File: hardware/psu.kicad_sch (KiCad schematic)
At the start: 59 parts, among them IC301 TLV61220DBVT, J301 54-00125, J302 Conn_01x03, Q301 CSD87503Q3E, Q302 CSD87503Q3E, Q303 Q_NMOS, U301 TPS63020DSJR, U302 BQ25798RQMR

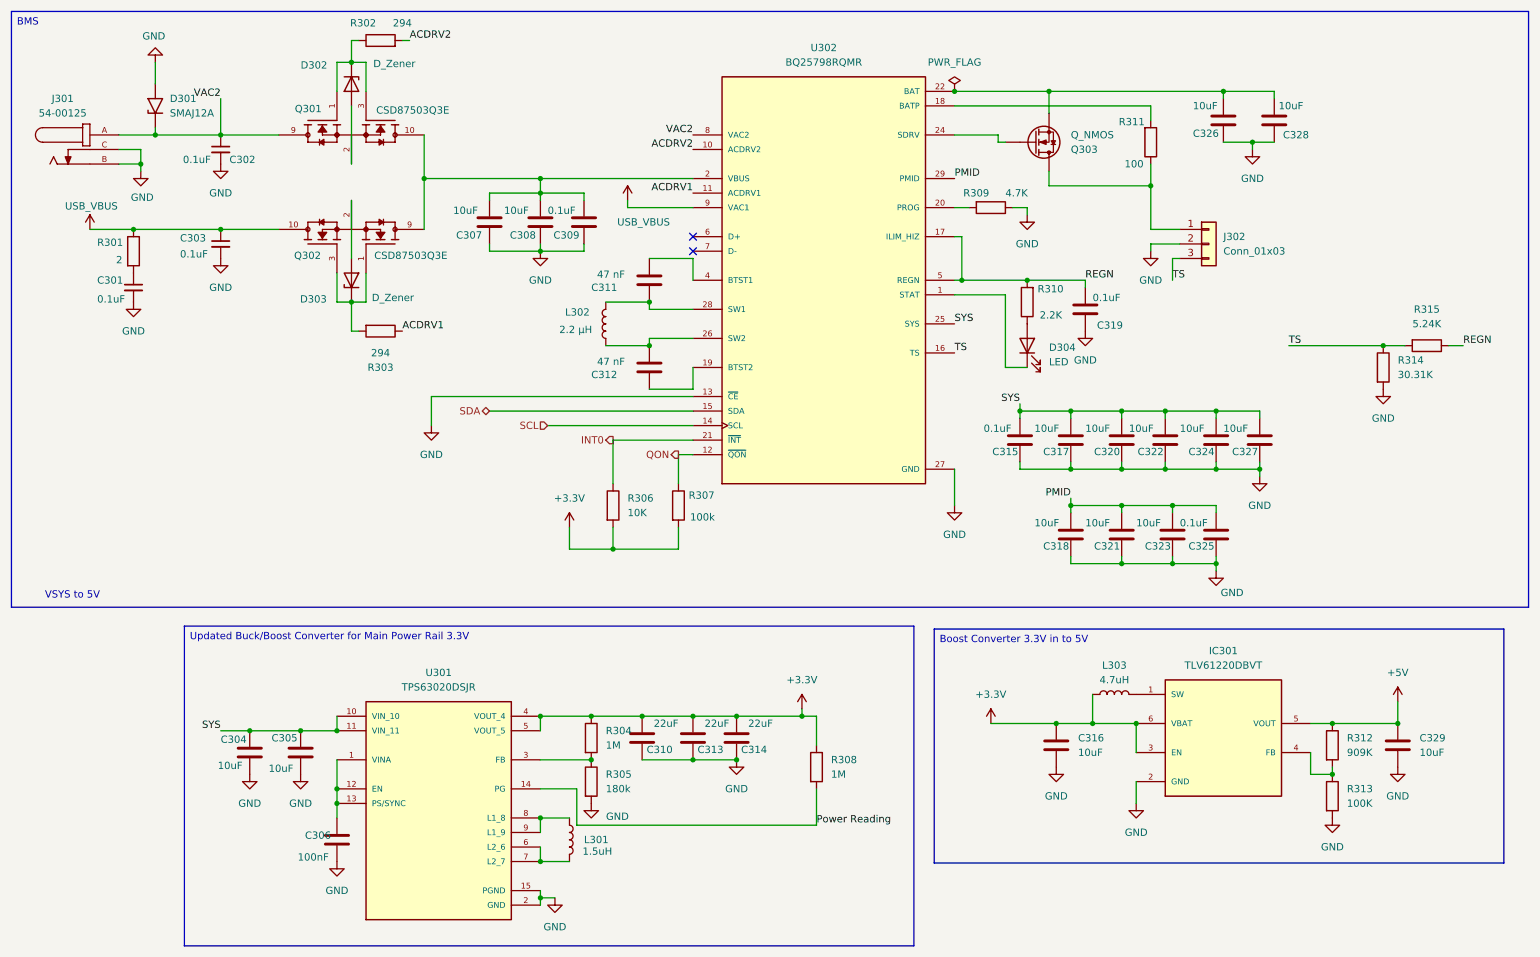
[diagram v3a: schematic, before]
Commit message: updated labels
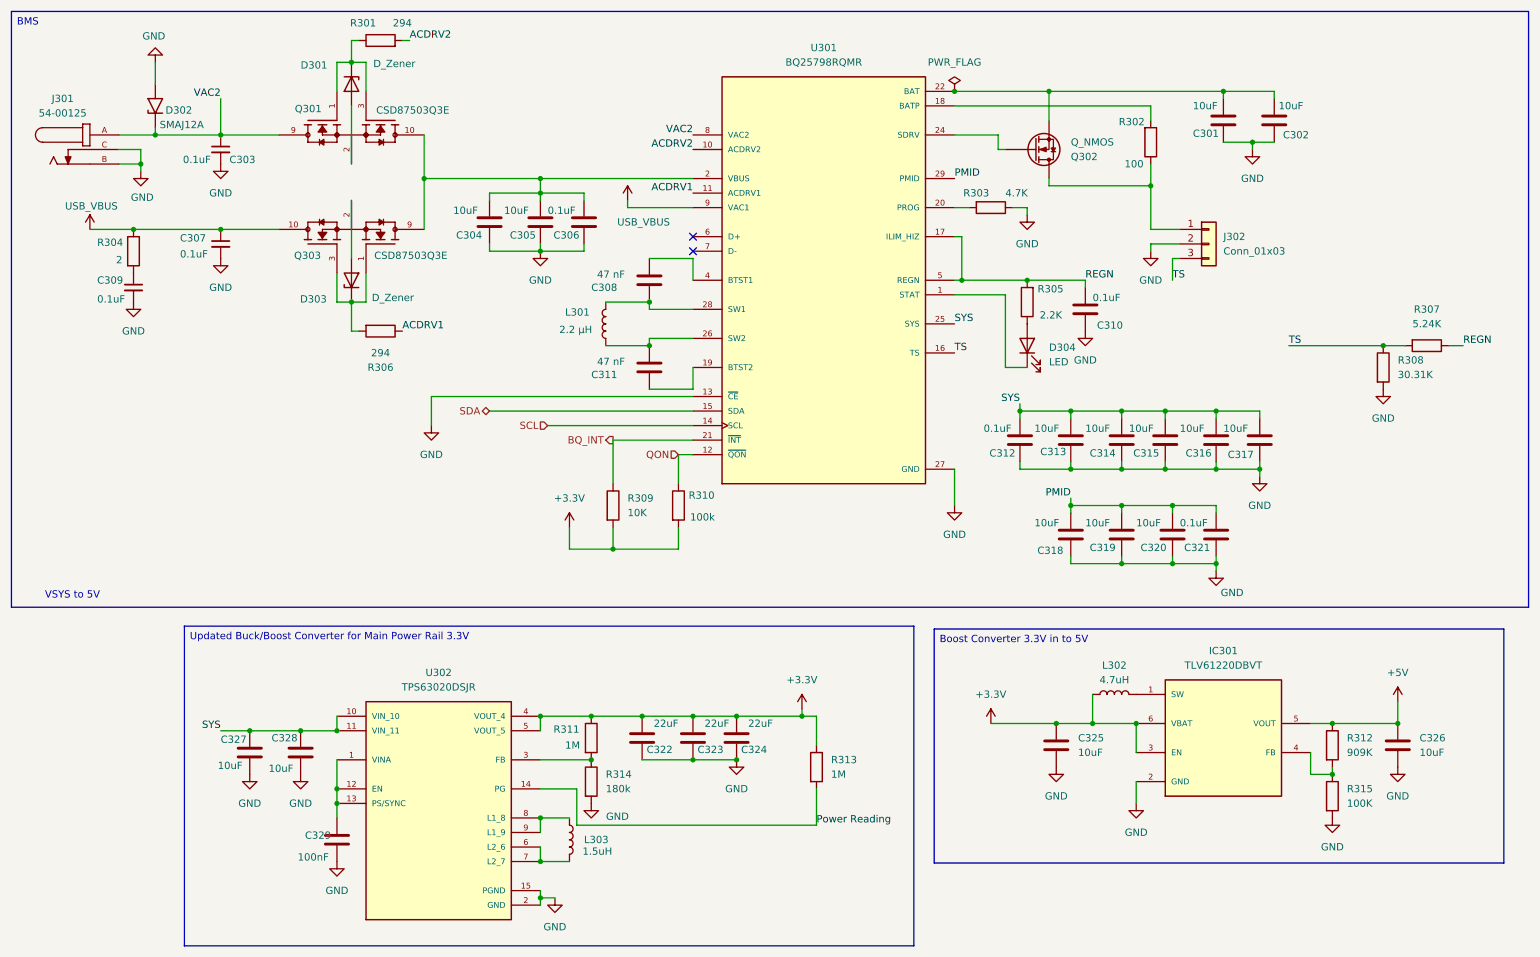
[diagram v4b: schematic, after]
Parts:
- renumbered C326 to C301, C328 to C302, C302 to C303, C307 to C304, C308 to C305, C309 to C306, C303 to C307, C311 to C308, C301 to C309, C319 to C310, C312 to C311, C315 to C312, C317 to C313, C320 to C314, C322 to C315, C324 to C316, C327 to C317, C321 to C319, C323 to C320, C325 to C321, C310 to C322, C313 to C323, C314 to C324, C316 to C325, C329 to C326, C304 to C327, C305 to C328, C306 to C329, D302 to D301, D301 to D302, L302 to L301, L303 to L302, L301 to L303, Q303 to Q302, Q302 to Q303, R302 to R301, R311 to R302, R309 to R303, R301 to R304, R310 to R305, R303 to R306, R315 to R307, R314 to R308, R306 to R309, R307 to R310, R304 to R311, R308 to R313, R305 to R314, R313 to R315, U302 to U301, U301 to U302
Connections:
- net INT0 renamed BQ_INT
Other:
- moved on the sheet: Q302

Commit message: reannotate
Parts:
- renumbered C301 to C201, C302 to C202, C303 to C203, C304 to C204, C305 to C205, C306 to C206, C307 to C207, C308 to C208, C309 to C209, C310 to C210, C311 to C211, C312 to C212, C313 to C213, C314 to C214, C315 to C215, C316 to C216, C317 to C217, C318 to C218, C319 to C219, C320 to C220, C321 to C221, C322 to C222, C323 to C223, C324 to C224, C325 to C225, C326 to C226, C327 to C227, C328 to C228, C329 to C229, D301 to D201, D302 to D202, D303 to D203, D304 to D204, IC301 to IC201, J301 to J201, J302 to J202, L301 to L201, L302 to L202, L303 to L203, Q301 to Q201, Q302 to Q202, Q303 to Q203, R301 to R201, R302 to R202, R303 to R203, R304 to R204, R305 to R205, R306 to R206, R307 to R207, R308 to R208, R309 to R209, R310 to R210, R311 to R211, R312 to R212, R313 to R213, R314 to R214, R315 to R215, U301 to U201, U302 to U202

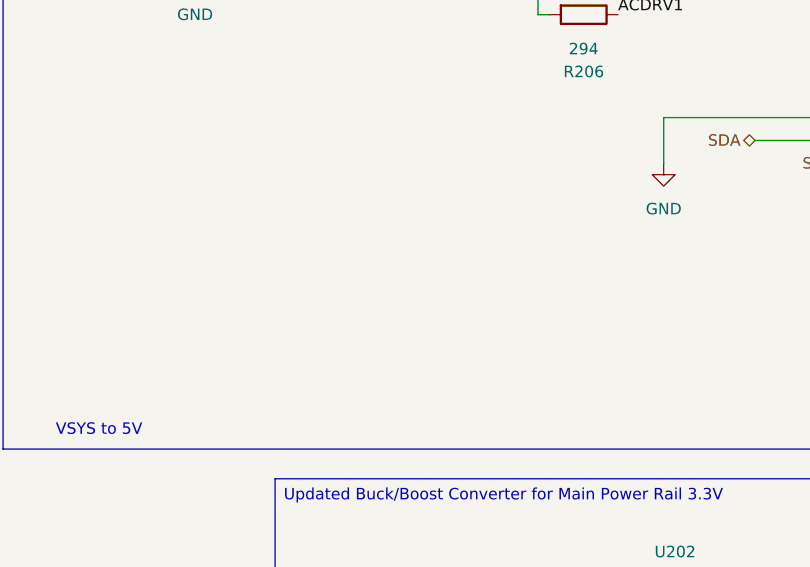
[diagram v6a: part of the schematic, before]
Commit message: added QON pushbutton
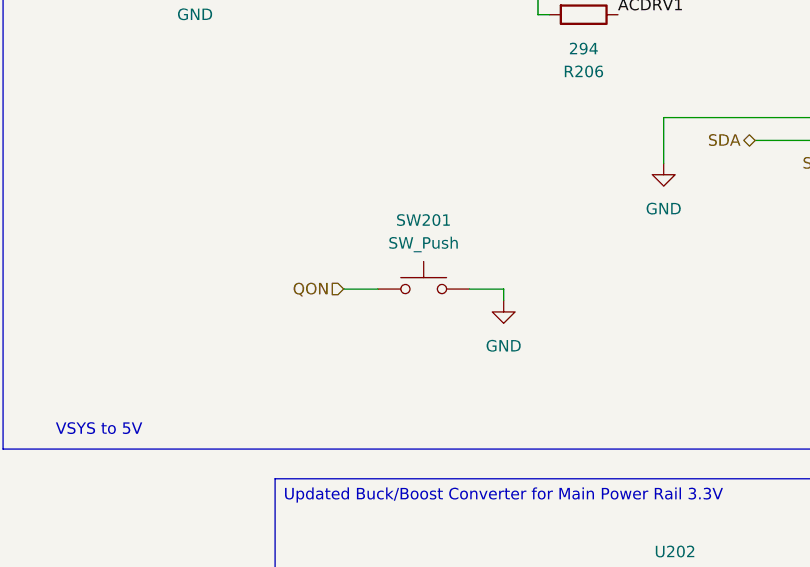
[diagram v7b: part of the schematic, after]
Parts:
- added SW201: SW_Push, symbol Switch:SW_Push
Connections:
- net GND: now also SW201.2
- net QON: now also SW201.1
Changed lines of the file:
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@@
 	(wire
 		(pts
+			(xy 67.31 100.33) (xy 71.12 100.33)
+		)
+		(stroke
+			(width 0)
+			(type default)
+		)
+	)
+	(wire
+		(pts
 			(xy 226.06 110.49) (xy 226.06 111.76)
 		)
@@
 	(wire
 		(pts
+			(xy 53.34 100.33) (xy 57.15 100.33)
+		)
+		(stroke
+			(width 0)
+			(type default)
+		)
+	)
+	(wire
+		(pts
 			(xy 217.17 93.98) (xy 226.06 93.98)
 		)
@@
 	(wire
 		(pts
+			(xy 71.12 100.33) (xy 71.12 101.6)
+		)
+		(stroke
+			(width 0)
+			(type default)
+		)
+	)
+	(wire
+		(pts
 			(xy 218.44 57.15) (xy 219.71 57.15)
 		)
@@
 		)
 	)
+	(hierarchical_label "QON"
+		(shape input)
+		(at 53.34 100.33 180)
+		(effects
+			(font
+				(size 1.27 1.27)
+			)
+			(justify right)
+		)
+	)
 	(symbol
 		(lib_id "Device:C")
@@
 	)
 	(symbol
+		(lib_id "power:GND")
+		(at 71.12 101.6 0)
+		(unit 1)
+		(exclude_from_sim no)
+		(in_bom yes)
+		(on_board yes)
+		(dnp no)
+		(fields_autoplaced yes)
+		(property "Reference" "#PWR0217"
+			(at 71.12 107.95 0)
+			(effects
+				(font
+					(size 1.27 1.27)
+				)
+				(hide yes)
+			)
+		)
+		(property "Value" "GND"
+			(at 71.12 106.68 0)
+			(effects
+				(font
+					(size 1.27 1.27)
+				)
+			)
+		)
+		(property "Footprint" ""
+			(at 71.12 101.6 0)
+			(effects
+				(font
+					(size 1.27 1.27)
+				)
+				(hide yes)
+			)
+		)
+		(property "Datasheet" ""
+			(at 71.12 101.6 0)
+			(effects
+				(font
+					(size 1.27 1.27)
+				)
+				(hide yes)
+			)
+		)
+		(property "Description" "Power symbol creates a global label with name \"GND\" , ground"
+			(at 71.12 101.6 0)
+			(effects
+				(font
+					(size 1.27 1.27)
+				)
+				(hide yes)
+			)
+		)
+		(pin "1"
+		)
+		(instances
+			(project "Senior_Design"
+				(path "/8f5928e8-0fc1-4443-a20f-3bfeb956761e/09dae378-4d12-4dca-bc21-c216f94ec21f"
+					(reference "#PWR0217")
+					(unit 1)
+				)
+			)
+		)
+	)
+	(symbol
 		(lib_id "Device:C_Small")
 		(at 52.07 38.1 0)
@@
 		(dnp no)
 		(fields_autoplaced yes)
-		(property "Reference" "#PWR0230"
+		(property "Reference" "#PWR0231"
 			(at 72.39 168.91 0)
 			(effects
@@
 			(project "Senior_Design"
 				(path "/8f5928e8-0fc1-4443-a20f-3bfeb956761e/09dae378-4d12-4dca-bc21-c216f94ec21f"
-					(reference "#PWR0230")
+					(reference "#PWR0231")
 					(unit 1)
 				)
@@
 		(dnp no)
 		(fields_autoplaced yes)
-		(property "Reference" "#PWR0228"
+		(property "Reference" "#PWR0229"
 			(at 212.09 158.75 0)
 			(effects
@@
 			(project "Senior_Design"
 				(path "/8f5928e8-0fc1-4443-a20f-3bfeb956761e/09dae378-4d12-4dca-bc21-c216f94ec21f"
-					(reference "#PWR0228")
+					(reference "#PWR0229")
 					(unit 1)
 				)
@@
 		(on_board yes)
 		(dnp no)
-		(property "Reference" "#PWR0218"
+		(property "Reference" "#PWR0219"
 			(at 226.06 118.11 0)
 			(effects
@@
 			(project "Senior_Design"
 				(path "/8f5928e8-0fc1-4443-a20f-3bfeb956761e/09dae378-4d12-4dca-bc21-c216f94ec21f"
-					(reference "#PWR0218")
+					(reference "#PWR0219")
 					(unit 1)
 				)
@@
 		(dnp no)
 		(fields_autoplaced yes)
-		(property "Reference" "#PWR0222"
+		(property "Reference" "#PWR0223"
 			(at 142.24 151.13 0)
 			(effects
@@
 			(project "Senior_Design"
 				(path "/8f5928e8-0fc1-4443-a20f-3bfeb956761e/09dae378-4d12-4dca-bc21-c216f94ec21f"
-					(reference "#PWR0222")
+					(reference "#PWR0223")
 					(unit 1)
 				)
@@
 		(dnp no)
 		(fields_autoplaced yes)
-		(property "Reference" "#PWR0221"
+		(property "Reference" "#PWR0222"
 			(at 186.69 142.24 0)
 			(effects
@@
 			(project "Senior_Design"
 				(path "/8f5928e8-0fc1-4443-a20f-3bfeb956761e/09dae378-4d12-4dca-bc21-c216f94ec21f"
-					(reference "#PWR0221")
+					(reference "#PWR0222")
 					(unit 1)
 				)
@@
 		(dnp no)
 		(fields_autoplaced yes)
-		(property "Reference" "#PWR0226"
+		(property "Reference" "#PWR0227"
 			(at 66.04 153.67 0)
 			(effects
@@
 			(project "Senior_Design"
 				(path "/8f5928e8-0fc1-4443-a20f-3bfeb956761e/09dae378-4d12-4dca-bc21-c216f94ec21f"
-					(reference "#PWR0226")
+					(reference "#PWR0227")
 					(unit 1)
 				)
@@
 		(dnp no)
 		(fields_autoplaced yes)
-		(property "Reference" "#PWR0219"
+		(property "Reference" "#PWR0220"
 			(at 257.81 138.43 0)
 			(effects
@@
 			(project ""
 				(path "/8f5928e8-0fc1-4443-a20f-3bfeb956761e/09dae378-4d12-4dca-bc21-c216f94ec21f"
-					(reference "#PWR0219")
+					(reference "#PWR0220")
 					(unit 1)
 				)
@@
 		(dnp no)
 		(fields_autoplaced yes)
-		(property "Reference" "#PWR0229"
+		(property "Reference" "#PWR0230"
 			(at 246.38 161.29 0)
 			(effects
@@
 			(project "Senior_Design"
 				(path "/8f5928e8-0fc1-4443-a20f-3bfeb956761e/09dae378-4d12-4dca-bc21-c216f94ec21f"
-					(reference "#PWR0229")
+					(reference "#PWR0230")
 					(unit 1)
 				)
@@
 		(dnp no)
 		(fields_autoplaced yes)
-		(property "Reference" "#PWR0231"
+		(property "Reference" "#PWR0232"
 			(at 110.49 175.26 0)
 			(effects
@@
 			(project "Senior_Design"
 				(path "/8f5928e8-0fc1-4443-a20f-3bfeb956761e/09dae378-4d12-4dca-bc21-c216f94ec21f"
-					(reference "#PWR0231")
+					(reference "#PWR0232")
 					(unit 1)
 				)
@@
 	)
 	(symbol
+		(lib_id "Switch:SW_Push")
+		(at 62.23 100.33 0)
+		(unit 1)
+		(exclude_from_sim no)
+		(in_bom yes)
+		(on_board yes)
+		(dnp no)
+		(fields_autoplaced yes)
+		(property "Reference" "SW201"
+			(at 62.23 92.71 0)
+			(effects
+				(font
+					(size 1.27 1.27)
+				)
+			)
+		)
+		(property "Value" "SW_Push"
+			(at 62.23 95.25 0)
+			(effects
+				(font
+					(size 1.27 1.27)
+				)
+			)
+		)
+		(property "Footprint" ""
+			(at 62.23 95.25 0)
+			(effects
+				(font
+					(size 1.27 1.27)
+				)
+				(hide yes)
+			)
+		)
+		(property "Datasheet" "~"
+			(at 62.23 95.25 0)
+			(effects
+				(font
+					(size 1.27 1.27)
+				)
+				(hide yes)
+			)
+		)
+		(property "Description" "Push button switch, generic, two pins"
+			(at 62.23 100.33 0)
+			(effects
+				(font
+					(size 1.27 1.27)
+				)
+				(hide yes)
+			)
+		)
+		(pin "2"
+		)
+		(pin "1"
+		)
+		(instances
+			(project ""
+				(path "/8f5928e8-0fc1-4443-a20f-3bfeb956761e/09dae378-4d12-4dca-bc21-c216f94ec21f"
+					(reference "SW201")
+					(unit 1)
+				)
+			)
+		)
+	)
+	(symbol
 		(lib_id "power:+3.3V")
 		(at 153.67 135.89 0)
@@
 		(dnp no)
 		(fields_autoplaced yes)
-		(property "Reference" "#PWR0220"
+		(property "Reference" "#PWR0221"
 			(at 153.67 139.7 0)
 			(effects
@@
 			(project "Senior_Design"
 				(path "/8f5928e8-0fc1-4443-a20f-3bfeb956761e/09dae378-4d12-4dca-bc21-c216f94ec21f"
-					(reference "#PWR0220")
+					(reference "#PWR0221")
 					(unit 1)
 				)
@@
 		(dnp no)
 		(fields_autoplaced yes)
-		(property "Reference" "#PWR0224"
+		(property "Reference" "#PWR0225"
 			(at 257.81 152.4 0)
 			(effects
@@
 			(project "Senior_Design"
 				(path "/8f5928e8-0fc1-4443-a20f-3bfeb956761e/09dae378-4d12-4dca-bc21-c216f94ec21f"
-					(reference "#PWR0224")
+					(reference "#PWR0225")
 					(unit 1)
 				)
@@
 		(dnp no)
 		(fields_autoplaced yes)
-		(property "Reference" "#PWR0225"
+		(property "Reference" "#PWR0226"
 			(at 57.15 153.67 0)
 			(effects
@@
 			(project "Senior_Design"
 				(path "/8f5928e8-0fc1-4443-a20f-3bfeb956761e/09dae378-4d12-4dca-bc21-c216f94ec21f"
-					(reference "#PWR0225")
+					(reference "#PWR0226")
 					(unit 1)
 				)
@@
 		(dnp no)
 		(fields_autoplaced yes)
-		(property "Reference" "#PWR0223"
+		(property "Reference" "#PWR0224"
 			(at 198.12 152.4 0)
 			(effects
@@
 			(project "Senior_Design"
 				(path "/8f5928e8-0fc1-4443-a20f-3bfeb956761e/09dae378-4d12-4dca-bc21-c216f94ec21f"
-					(reference "#PWR0223")
+					(reference "#PWR0224")
 					(unit 1)
 				)
@@
 		(on_board yes)
 		(dnp no)
-		(property "Reference" "#PWR0227"
+		(property "Reference" "#PWR0228"
 			(at 116.84 158.75 0)
 			(effects
@@
 			(project "Senior_Design"
 				(path "/8f5928e8-0fc1-4443-a20f-3bfeb956761e/09dae378-4d12-4dca-bc21-c216f94ec21f"
-					(reference "#PWR0227")
+					(reference "#PWR0228")
 					(unit 1)
 				)
@@
 		(dnp no)
 		(fields_autoplaced yes)
-		(property "Reference" "#PWR0217"
+		(property "Reference" "#PWR0218"
 			(at 113.03 107.95 0)
 			(effects
@@
 			(project "Senior_Design"
 				(path "/8f5928e8-0fc1-4443-a20f-3bfeb956761e/09dae378-4d12-4dca-bc21-c216f94ec21f"
-					(reference "#PWR0217")
+					(reference "#PWR0218")
 					(unit 1)
 				)

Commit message: PCB footprint update
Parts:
- SW201: footprint (none) -> Button_Switch_SMD:SW_SPST_TL3305A
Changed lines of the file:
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@@
 			)
 		)
-		(property "Footprint" ""
+		(property "Footprint" "Button_Switch_SMD:SW_SPST_TL3305A"
 			(at 62.23 95.25 0)
 			(effects
